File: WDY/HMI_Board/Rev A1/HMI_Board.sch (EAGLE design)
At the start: 30 parts, among them SW1 B3FS-1015, SW2 B3FS-1015, SW3 B3FS-1015, SW4 B3FS-1015, SW5 B3FS-1015, SW6 B3FS-1015, U1 90814-0208, U2 90814-0206

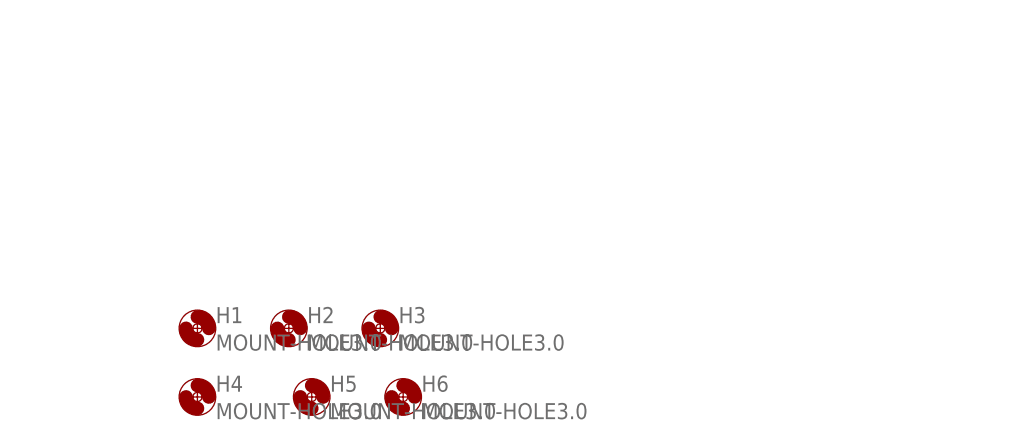
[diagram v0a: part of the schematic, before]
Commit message: Panelize the board, add fiducial
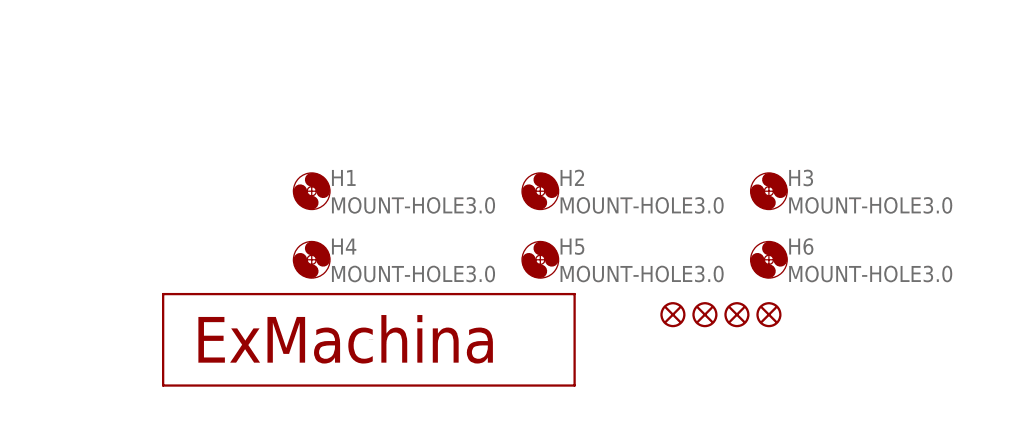
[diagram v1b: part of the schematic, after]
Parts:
- added JP1, JP2, JP3, JP4: FIDUCIAL1X2, SparkFun:FIDUCIAL1X2
- added U$1: EXMACHINA-LOGO-NAME, exmachina:EXMACHINA-LOGO-NAME
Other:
- moved on the sheet: H1, H2, H3, H4, H5, H6
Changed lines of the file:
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@@
 </class>
 <class number="2" name="supply" width="0.4064" drill="0.5">
-<clearance class="2" value="0.127"/>
 </class>
 </classes>
@@
 <part name="TP1" library="testpad" deviceset="TP" device="B2,54"/>
 <part name="TP2" library="testpad" deviceset="TP" device="B2,54"/>
+<part name="U$1" library="exmachina" deviceset="EXMACHINA-LOGO" device="-NAME"/>
+<part name="JP1" library="SparkFun" deviceset="FIDUCIAL" device="1X2"/>
+<part name="JP2" library="SparkFun" deviceset="FIDUCIAL" device="1X2"/>
+<part name="JP3" library="SparkFun" deviceset="FIDUCIAL" device="1X2"/>
+<part name="JP4" library="SparkFun" deviceset="FIDUCIAL" device="1X2"/>
 </parts>
 <sheets>
@@
 <instance part="+3V8" gate="G$1" x="27.94" y="228.6"/>
 <instance part="GND12" gate="1" x="73.66" y="208.28"/>
-<instance part="H1" gate="G$1" x="292.1" y="20.32"/>
-<instance part="H2" gate="G$1" x="302.26" y="20.32"/>
-<instance part="H3" gate="G$1" x="312.42" y="20.32"/>
-<instance part="H4" gate="G$1" x="292.1" y="12.7"/>
-<instance part="H5" gate="G$1" x="304.8" y="12.7"/>
-<instance part="H6" gate="G$1" x="314.96" y="12.7"/>
+<instance part="H1" gate="G$1" x="304.8" y="35.56"/>
+<instance part="H2" gate="G$1" x="330.2" y="35.56"/>
+<instance part="H3" gate="G$1" x="355.6" y="35.56"/>
+<instance part="H4" gate="G$1" x="304.8" y="27.94"/>
+<instance part="H5" gate="G$1" x="330.2" y="27.94"/>
+<instance part="H6" gate="G$1" x="355.6" y="27.94"/>
 <instance part="TP1" gate="G$1" x="30.48" y="228.6"/>
 <instance part="TP2" gate="G$1" x="81.28" y="205.74" rot="R180"/>
+<instance part="U$1" gate="G$1" x="311.15" y="19.05"/>
+<instance part="JP1" gate="G$1" x="344.932" y="21.844"/>
+<instance part="JP2" gate="G$1" x="348.488" y="21.844"/>
+<instance part="JP3" gate="G$1" x="352.044" y="21.844"/>
+<instance part="JP4" gate="G$1" x="355.6" y="21.844"/>
 </instances>
 <busses>

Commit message: Add value on LED
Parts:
- LED1, LED2, LED3, LED4: value (none) -> Blue
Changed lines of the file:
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@@
 <classes>
 <class number="0" name="default" width="0" drill="0">
-<clearance class="0" value="0.205"/>
 </class>
 <class number="1" name="signal" width="0.1778" drill="0.35">
-<clearance class="0" value="0.205"/>
-<clearance class="1" value="0.205"/>
 </class>
 <class number="2" name="supply" width="0.4064" drill="0.5">
-<clearance class="0" value="0.205"/>
-<clearance class="1" value="0.205"/>
-<clearance class="2" value="0.205"/>
 </class>
 </classes>
 <parts>
 <part name="FRAME1" library="frames" deviceset="A3L-LOC" device=""/>
-<part name="LED1" library="led" deviceset="LED" device="SML0603"/>
-<part name="LED2" library="led" deviceset="LED" device="SML0603"/>
-<part name="LED3" library="led" deviceset="LED" device="SML0603"/>
-<part name="LED4" library="led" deviceset="LED" device="SML0603"/>
+<part name="LED1" library="led" deviceset="LED" device="SML0603" value="Blue"/>
+<part name="LED2" library="led" deviceset="LED" device="SML0603" value="Blue"/>
+<part name="LED3" library="led" deviceset="LED" device="SML0603" value="Blue"/>
+<part name="LED4" library="led" deviceset="LED" device="SML0603" value="Blue"/>
 <part name="R1" library="rcl" deviceset="R-EU_" device="R0603" value="1k"/>
 <part name="R2" library="rcl" deviceset="R-EU_" device="R0603" value="1k"/>
@@
 </busses>
 <nets>
-<net name="GND" class="0">
+<net name="GND" class="2">
 <segment>
 <pinref part="GND1" gate="1" pin="GND"/>

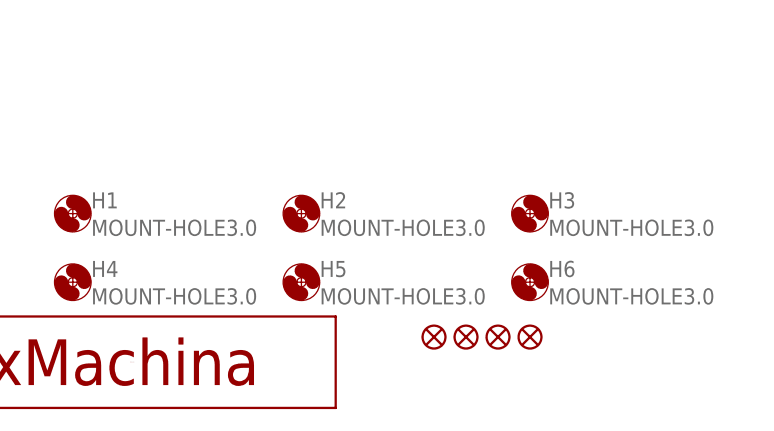
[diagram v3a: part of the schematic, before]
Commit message: Change LED position and generate gerber
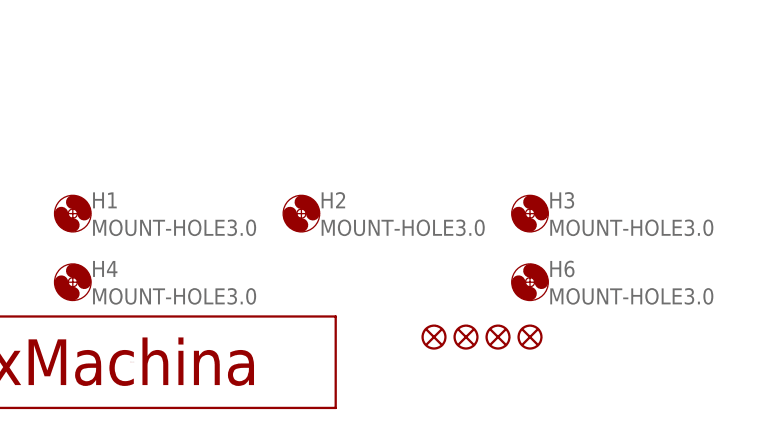
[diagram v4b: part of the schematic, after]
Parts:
- removed H5: MOUNT-HOLE3.0, holes:MOUNT-HOLE3.0
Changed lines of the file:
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@@
 <part name="H3" library="holes" deviceset="MOUNT-HOLE" device="3.0"/>
 <part name="H4" library="holes" deviceset="MOUNT-HOLE" device="3.0"/>
-<part name="H5" library="holes" deviceset="MOUNT-HOLE" device="3.0"/>
 <part name="H6" library="holes" deviceset="MOUNT-HOLE" device="3.0"/>
 <part name="TP1" library="testpad" deviceset="TP" device="B2,54"/>
@@
 <instance part="H3" gate="G$1" x="355.6" y="35.56"/>
 <instance part="H4" gate="G$1" x="304.8" y="27.94"/>
-<instance part="H5" gate="G$1" x="330.2" y="27.94"/>
 <instance part="H6" gate="G$1" x="355.6" y="27.94"/>
 <instance part="TP1" gate="G$1" x="30.48" y="228.6"/>
